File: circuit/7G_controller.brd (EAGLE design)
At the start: 63 x 70.5 mm, 22 parts, among them Q1 32768Hz, T1 TPS1101D

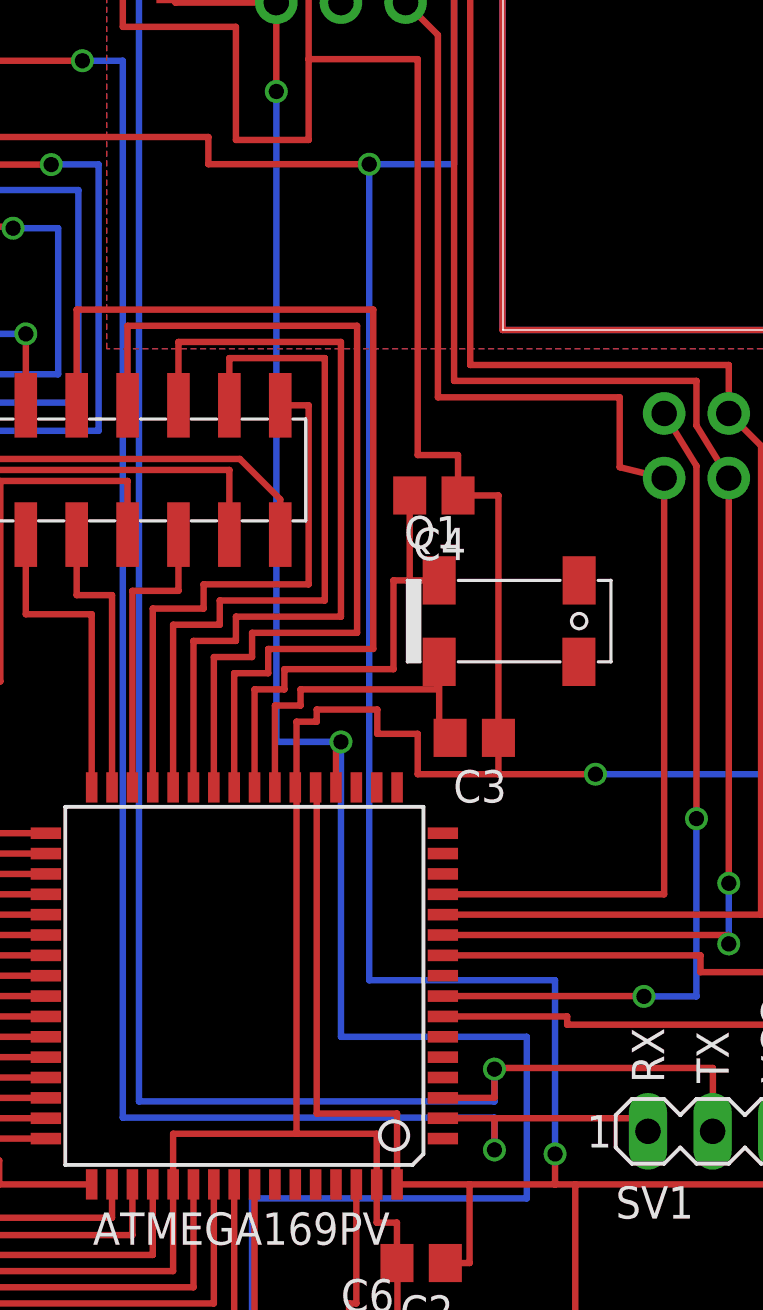
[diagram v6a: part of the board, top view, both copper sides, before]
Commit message: 
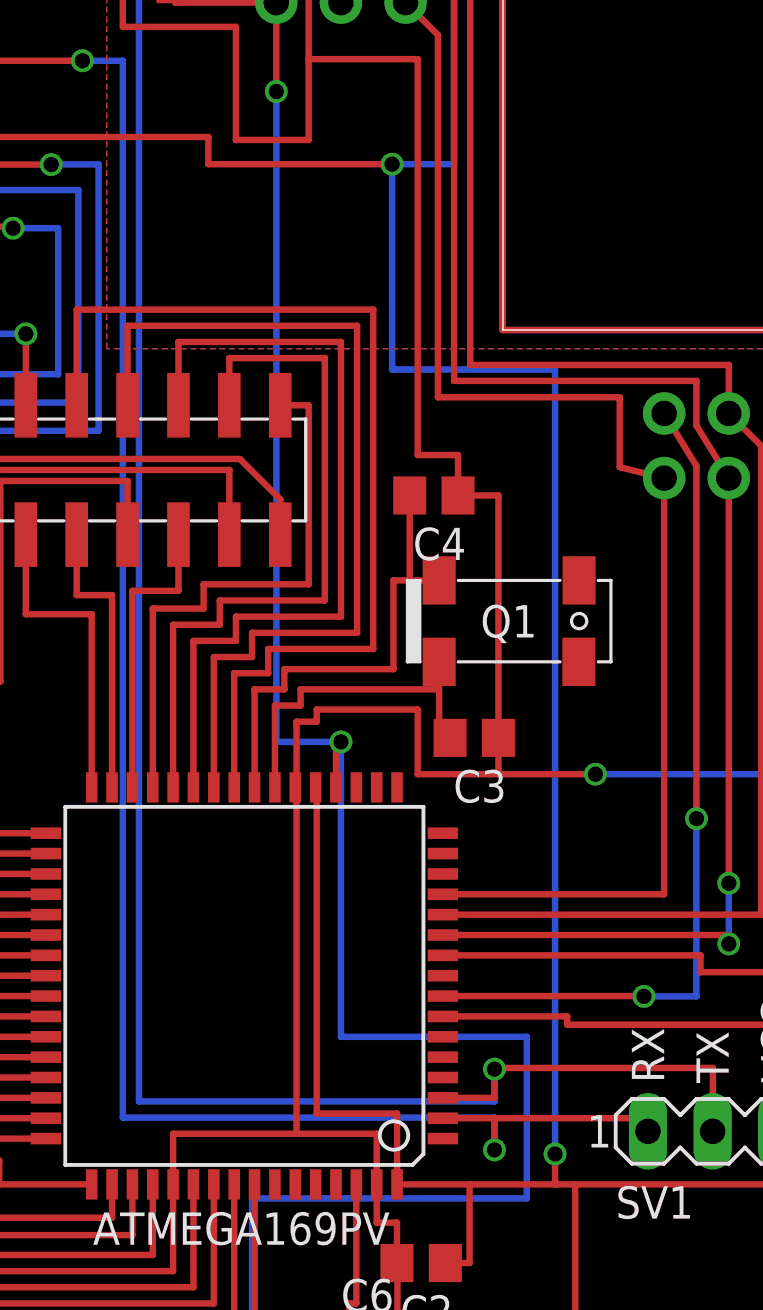
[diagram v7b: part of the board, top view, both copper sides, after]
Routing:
- net VCC: track 297.0 -> 296.1 mm
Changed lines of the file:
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@@
 <setting verticaltext="up"/>
 </settings>
-<grid distance="0.1" unitdist="mm" unit="mm" style="lines" multiple="1" display="yes" altdistance="0.025" altunitdist="inch" altunit="inch"/>
+<grid distance="0.5" unitdist="mm" unit="mm" style="lines" multiple="1" display="yes" altdistance="0.025" altunitdist="inch" altunit="inch"/>
 <layers>
 <layer number="1" name="Top" color="4" fill="1" visible="yes" active="yes"/>
@@
 <element name="C1" library="rcl" package="SMC_B" value="10uF" x="39.7225" y="10.19125" rot="R180"/>
 <element name="C2" library="rcl" package="C0805" value="100nF" x="35.53625" y="13.335" rot="R180"/>
-<element name="Q1" library="KileParts" package="NSK_QUARTZ_CLOCK" value="32768Hz" x="38.995" y="38.56"/>
+<element name="Q1" library="KileParts" package="NSK_QUARTZ_CLOCK" value="32768Hz" x="38.995" y="38.56" smashed="yes">
+<attribute name="NAME" x="37.8675" y="37.9175" size="1.27" layer="21"/>
+</element>
 <element name="C3" library="rcl" package="C0805" value="22pF" x="37.62375" y="33.9725" rot="R180"/>
 <element name="C4" library="rcl" package="C0805" value="22pF" x="36.03625" y="43.4975" rot="R180"/>
@@
 <wire x1="31.4325" y1="19.20875" x2="34.59" y2="19.20875" width="0.254" layer="1"/>
 <wire x1="34.59" y1="19.20875" x2="34.59" y2="16.425" width="0.254" layer="1"/>
-<via x="33.49625" y="56.515" extent="1-16" drill="0.6" shape="square"/>
-<wire x1="33.49625" y1="56.515" x2="33.49625" y2="24.4475" width="0.254" layer="16"/>
-<wire x1="33.49625" y1="24.4475" x2="40.79875" y2="24.4475" width="0.254" layer="16"/>
-<wire x1="40.79875" y1="24.4475" x2="40.79875" y2="17.62125" width="0.254" layer="16"/>
+<via x="34.39625" y="56.515" extent="1-16" drill="0.6" shape="square"/>
+<wire x1="34.39625" y1="56.515" x2="34.39625" y2="48.4475" width="0.254" layer="16"/>
+<wire x1="34.39625" y1="48.4475" x2="40.79875" y2="48.4475" width="0.254" layer="16"/>
+<wire x1="40.79875" y1="48.4475" x2="40.79875" y2="17.62125" width="0.254" layer="16"/>
 <via x="40.79875" y="17.62125" extent="1-16" drill="0.6" shape="square"/>
 <wire x1="10" y1="57.58375" x2="27.175" y2="57.58375" width="0.254" layer="1"/>
 <wire x1="34.925" y1="65.405" x2="36.83" y2="65.405" width="0.254" layer="16"/>
 <wire x1="36.83" y1="65.405" x2="36.83" y2="56.515" width="0.254" layer="16"/>
-<wire x1="36.83" y1="56.515" x2="33.49625" y2="56.515" width="0.254" layer="16"/>
+<wire x1="36.83" y1="56.515" x2="34.39625" y2="56.515" width="0.254" layer="16"/>
 <wire x1="32.86125" y1="64.135" x2="34.925" y2="65.405" width="0.254" layer="1"/>
 <wire x1="27.175" y1="57.58375" x2="27.175" y2="56.515" width="0.254" layer="1"/>
-<wire x1="27.175" y1="56.515" x2="33.49625" y2="56.515" width="0.254" layer="1"/>
+<wire x1="27.175" y1="56.515" x2="34.39625" y2="56.515" width="0.254" layer="1"/>
 <contactref element="NRF24L01" pad="+3.3V"/>
 <contactref element="C5" pad="+"/>
@@
 <wire x1="30.63875" y1="34.6075" x2="31.4325" y2="34.6075" width="0.254" layer="1"/>
 <wire x1="31.4325" y1="34.6075" x2="31.4325" y2="35.08375" width="0.254" layer="1"/>
-<wire x1="31.4325" y1="35.08375" x2="33.81375" y2="35.08375" width="0.254" layer="1"/>
-<wire x1="33.81375" y1="35.08375" x2="33.81375" y2="34.13125" width="0.254" layer="1"/>
 <wire x1="52.705" y1="44.18" x2="52.705" y2="42.0675" width="0.254" layer="1"/>
 <via x="52.705" y="32.22625" extent="1-16" drill="0.6" shape="square"/>
@@
 <wire x1="36.98625" y1="43.4975" x2="38.57375" y2="43.4975" width="0.254" layer="1"/>
 <wire x1="38.57375" y1="43.4975" x2="38.57375" y2="33.9725" width="0.254" layer="1"/>
-<wire x1="33.81375" y1="34.13125" x2="35.40125" y2="34.13125" width="0.254" layer="1"/>
-<wire x1="35.40125" y1="34.13125" x2="35.40125" y2="32.54375" width="0.254" layer="1"/>
+<wire x1="35.40125" y1="35.08375" x2="35.40125" y2="32.54375" width="0.254" layer="1"/>
 <wire x1="35.40125" y1="32.54375" x2="38.57375" y2="32.54375" width="0.254" layer="1"/>
 <wire x1="38.57375" y1="32.54375" x2="38.57375" y2="33.9725" width="0.254" layer="1"/>
@@
 <wire x1="52.705" y1="21.235" x2="52.07" y2="21.235" width="0.254" layer="1"/>
 <wire x1="52.07" y1="21.235" x2="52.07" y2="18.51" width="0.254" layer="1"/>
+<wire x1="31.4325" y1="35.08375" x2="35.40125" y2="35.08375" width="0.254" layer="1"/>
 </signal>
 <signal name="MOSI">

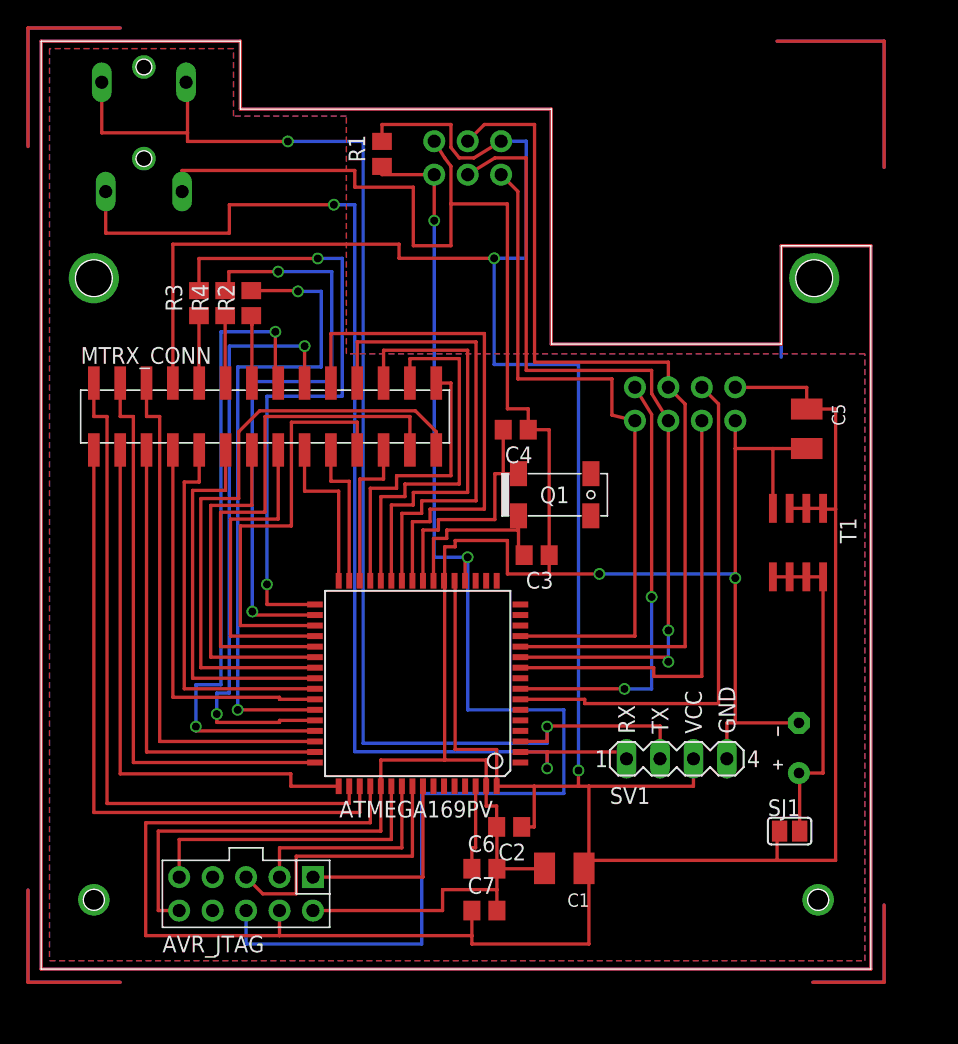
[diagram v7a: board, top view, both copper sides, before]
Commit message: CR2032 holder
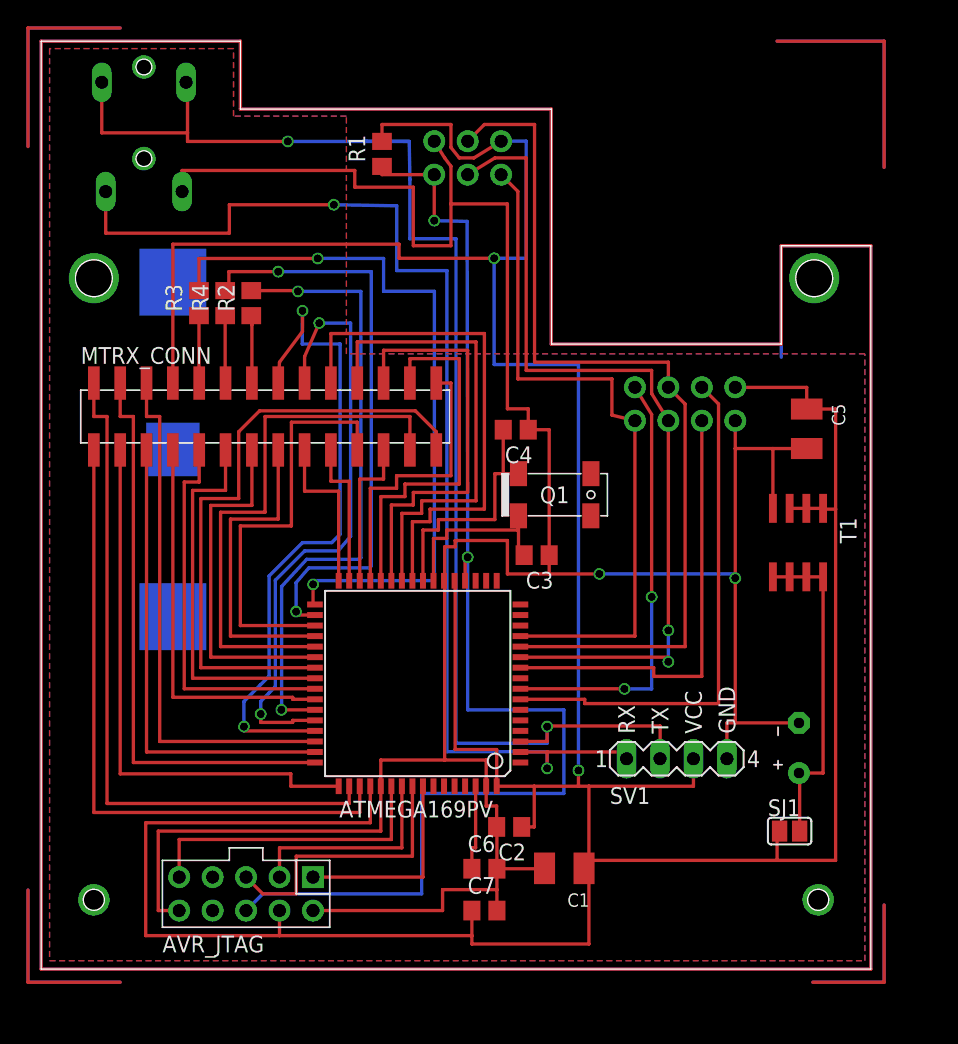
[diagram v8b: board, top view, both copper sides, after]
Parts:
- added U$1: (no value), adafruit:CR2032-SMD
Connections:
- net GND: now also U$1.-
- net N$4: now also U$1.+$1, U$1.+$2
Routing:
- net NUML: track 49.0 -> 56.0 mm
- net RESET: track 101.5 -> 95.6 mm
- net N$30: track 103.4 -> 106.9 mm
- net CAPS: track 49.4 -> 47.5 mm
- net SCRL: track 46.4 -> 45.1 mm
- net L8: track 49.5 -> 50.6 mm
